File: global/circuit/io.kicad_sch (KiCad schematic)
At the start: 8 parts, among them J1 AudioJack2_Ground, J2 AudioJack2_Ground, J3 USB4125-GF-A-0190, SW1 SW_DPDT_x2

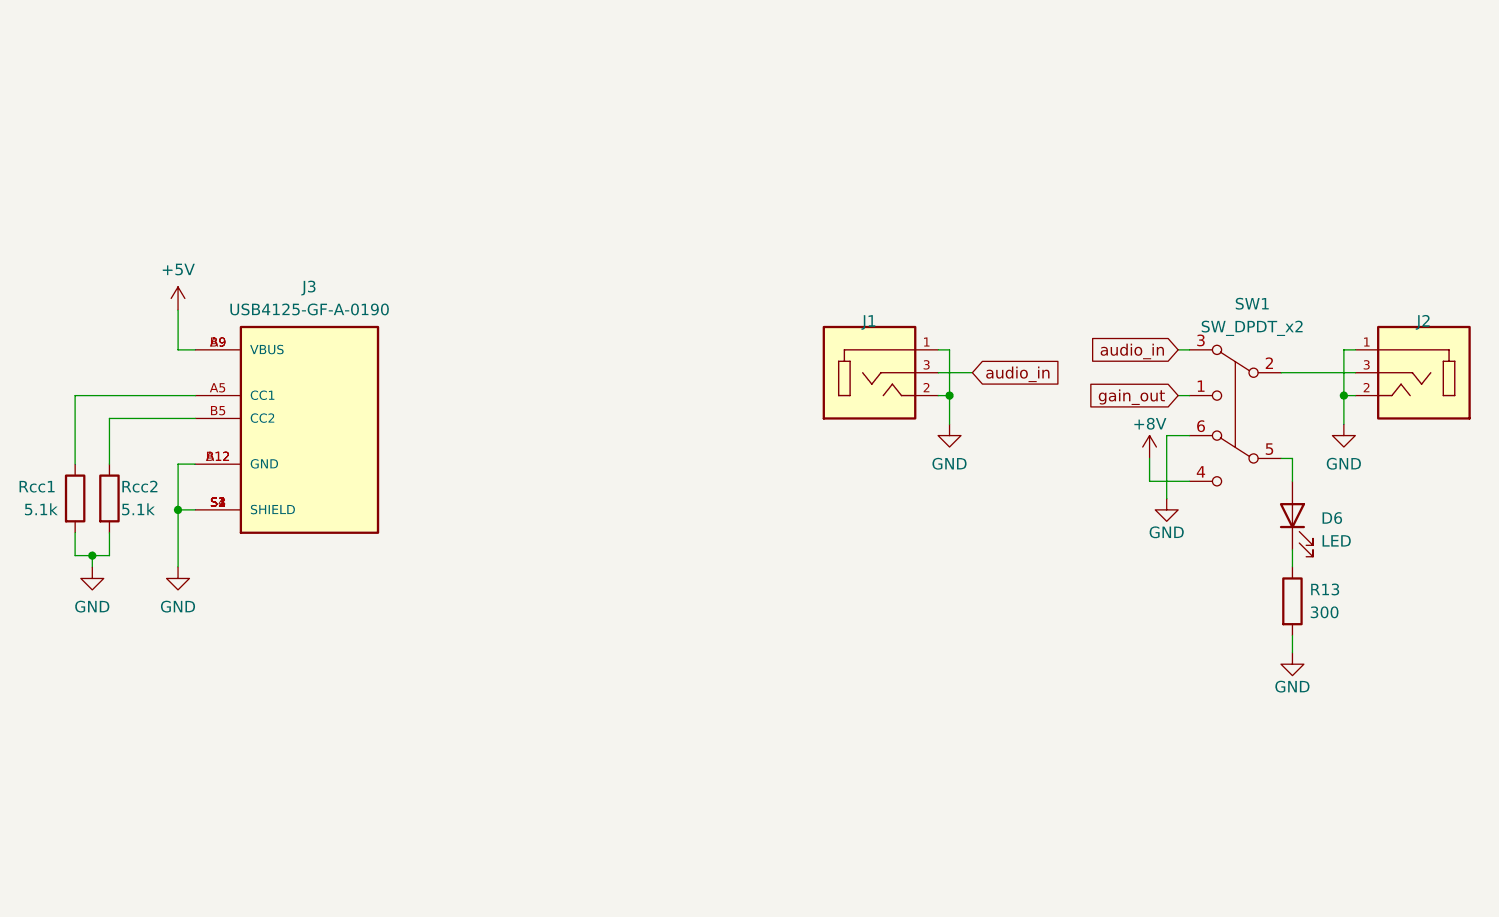
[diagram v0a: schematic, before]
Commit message: rework distortion circuit and simulations
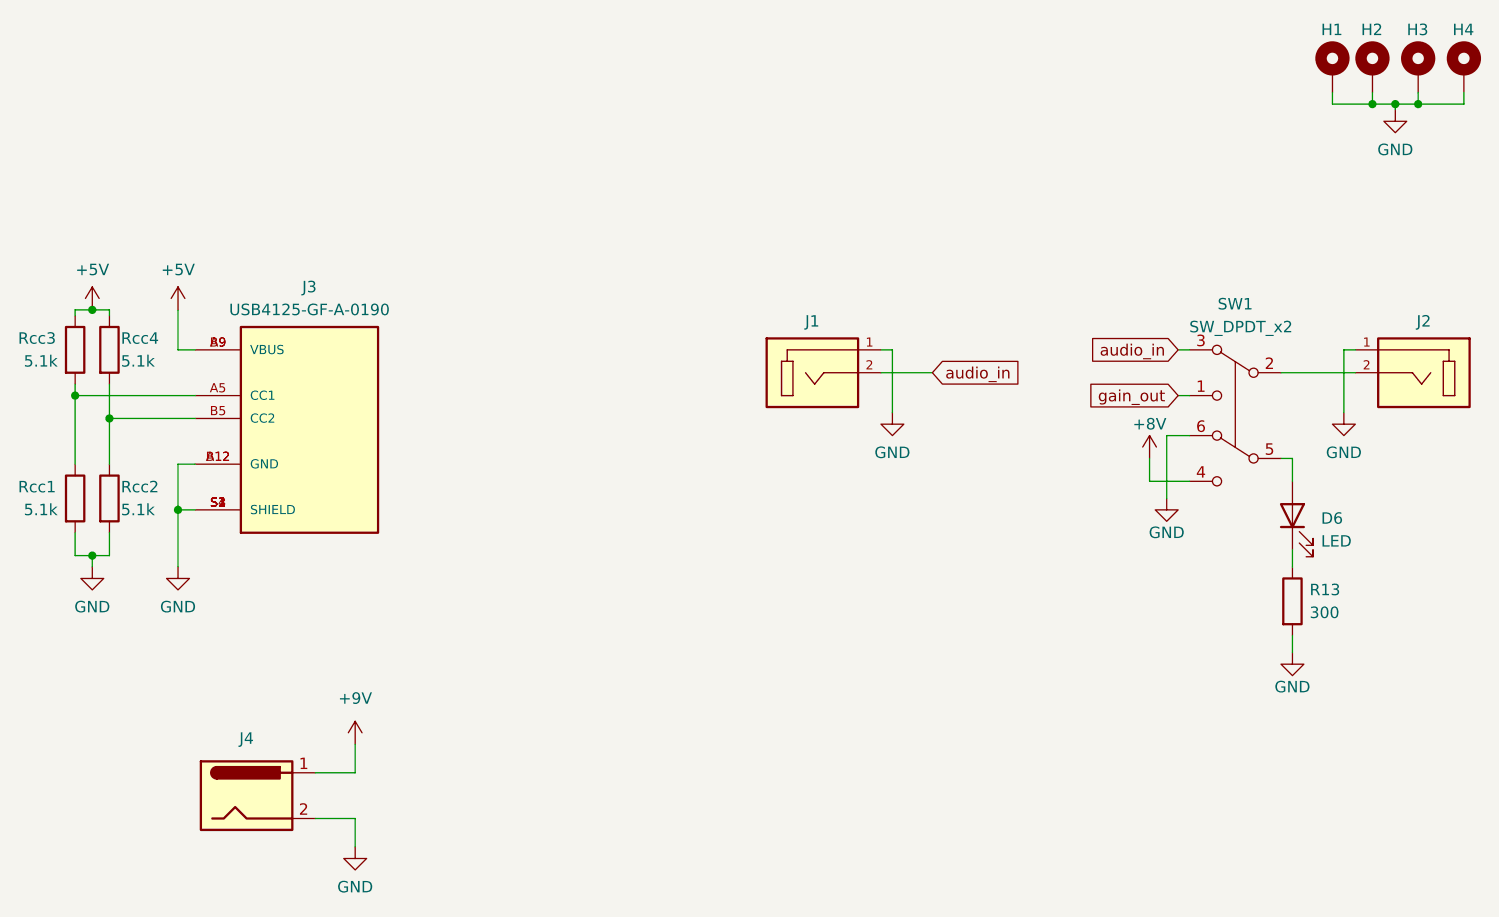
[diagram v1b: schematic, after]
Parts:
- added H1, H2, H3, H4: MountingHole_Pad, MountingHole:MountingHole_2.2mm_M2_DIN965_Pad_TopBottom, symbol Mechanical:MountingHole_Pad
- added J4: Barrel_Jack, Connector_PinHeader_2.54mm:PinHeader_1x02_P2.54mm_Vertical, symbol Connector:Barrel_Jack
- added Rcc3, Rcc4: 5.1k, Resistor_SMD:R_0805_2012Metric_Pad1.20x1.40mm_HandSolder, symbol Device:R
- D6: footprint effect_pedal:FB_28C0236-0EW-10 -> Connector_PinHeader_2.54mm:PinHeader_1x02_P2.54mm_Vertical
- J1, J2: footprint effect_pedal:CUI_SJ-3523-SMT-TR-V2 -> Connector_PinHeader_2.54mm:PinHeader_1x02_P2.54mm_Vertical; symbol effect_pedal:SJ-3523-SMT-TR -> effect_pedal:audio_jack_1_GND
- SW1: footprint effect_pedal:SF12011F020220RL050 -> Connector_PinHeader_2.54mm:PinHeader_2x03_P2.54mm_Vertical
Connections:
- net +5V: now also Rcc3.1, Rcc4.1
- net GND: now also H1.1, H2.1, H3.1, H4.1, J4.2; no longer J1.2, J2.2
- net audio_in: now also J1.2; no longer J1.3
- net at J3.A5 (CC1), Rcc1.1: now also Rcc3.2
- net at J3.B5 (CC2), Rcc2.1: now also Rcc4.2
- net at SW1.2: now also J2.2; no longer J2.3
- new net +9V: J4.1

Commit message: distortion rev 3
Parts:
- D6: footprint Connector_PinHeader_2.54mm:PinHeader_1x02_P2.54mm_Vertical -> effect_pedal:led_wired_1_pin
- J1: footprint Connector_PinHeader_2.54mm:PinHeader_1x02_P2.54mm_Vertical -> effect_pedal:audio_jack_wired
- J2: footprint Connector_PinHeader_2.54mm:PinHeader_1x02_P2.54mm_Vertical -> effect_pedal:audio_jack_wired_shield_only
- SW1: footprint Connector_PinHeader_2.54mm:PinHeader_2x03_P2.54mm_Vertical -> effect_pedal:switch_wired_reduced
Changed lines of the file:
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@@
       (effects (font (size 1.27 1.27)) hide)
     )
-    (property "Footprint" "Connector_PinHeader_2.54mm:PinHeader_1x02_P2.54mm_Vertical" (id 2) (at 111.125 55.88 0)
+    (property "Footprint" "effect_pedal:audio_jack_wired" (id 2) (at 111.125 55.88 0)
       (effects (font (size 1.27 1.27)) hide)
     )
@@
       (effects (font (size 1.27 1.27)) hide)
     )
-    (property "Footprint" "Connector_PinHeader_2.54mm:PinHeader_1x02_P2.54mm_Vertical" (id 2) (at 179.07 55.88 0)
+    (property "Footprint" "effect_pedal:audio_jack_wired_shield_only" (id 2) (at 179.07 55.88 0)
       (effects (font (size 1.27 1.27)) hide)
     )
@@
     (property "Reference" "SW1" (id 0) (at 158.115 48.26 0))
     (property "Value" "SW_DPDT_x2" (id 1) (at 158.75 50.8 0))
-    (property "Footprint" "Connector_PinHeader_2.54mm:PinHeader_2x03_P2.54mm_Vertical" (id 2) (at 133.35 53.34 0)
+    (property "Footprint" "effect_pedal:switch_wired_reduced" (id 2) (at 133.35 53.34 0)
       (effects (font (size 1.27 1.27)) (justify left) hide)
     )
@@
       (effects (font (size 1.27 1.27)) (justify right))
     )
-    (property "Footprint" "Connector_PinHeader_2.54mm:PinHeader_1x02_P2.54mm_Vertical" (id 2) (at 164.465 71.755 0)
-      (effects (font (size 1.27 1.27)) hide)
-    )
+    (property "Footprint" "effect_pedal:led_wired_1_pin" (id 2) (at 164.465 71.755 0)
+      (effects (font (size 1.27 1.27)) hide)
+    )

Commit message: rework global circuits
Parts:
- J?: renamed from J4; footprint Connector_PinHeader_2.54mm:PinHeader_1x02_P2.54mm_Vertical -> effect_pedal:barrel_jack_wired
- J?: renamed from J2; footprint effect_pedal:audio_jack_wired_shield_only -> effect_pedal:audio_jack_wired
- SW?: renamed from SW1; footprint effect_pedal:switch_wired_reduced -> effect_pedal:switch_wired
- renumbered D6 to D?, H3 to H?, H4 to H?, H1 to H?, H2 to H?, J1 to J?, J3 to J?, R13 to R?, Rcc4 to Rcc?, Rcc1 to Rcc?, Rcc2 to Rcc?, Rcc3 to Rcc?
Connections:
- net gain_out renamed effect_out
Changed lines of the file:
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@@
     )
   )
-  (global_label "gain_out" (shape input) (at 151.765 58.42 180) (fields_autoplaced)
+  (global_label "effect_out" (shape input) (at 151.765 58.42 180) (fields_autoplaced)
     (effects (font (size 1.27 1.27)) (justify right))
-    (property "Intersheet References" "${INTERSHEET_REFS}" (id 0) (at 141.3086 58.3406 0)
+    (property "Intersheet References" "${INTERSHEET_REFS}" (id 0) (at 139.9176 58.3406 0)
       (effects (font (size 1.27 1.27)) (justify right) hide)
     )
@@
   (symbol (lib_id "power:GND") (at 120.015 60.325 0) (unit 1)
     (in_bom yes) (on_board yes)
-    (property "Reference" "#PWR0109" (id 0) (at 120.015 66.675 0)
+    (property "Reference" "#PWR?" (id 0) (at 120.015 66.675 0)
       (effects (font (size 1.27 1.27)) hide)
     )
@@
   (symbol (lib_id "power:GND") (at 150.495 69.85 0) (unit 1)
     (in_bom yes) (on_board yes)
-    (property "Reference" "#PWR026" (id 0) (at 150.495 76.2 0)
+    (property "Reference" "#PWR?" (id 0) (at 150.495 76.2 0)
       (effects (font (size 1.27 1.27)) hide)
     )
@@
   (symbol (lib_id "power:+5V") (at 31.115 48.895 0) (unit 1)
     (in_bom yes) (on_board yes)
-    (property "Reference" "#PWR028" (id 0) (at 31.115 52.705 0)
+    (property "Reference" "#PWR?" (id 0) (at 31.115 52.705 0)
       (effects (font (size 1.27 1.27)) hide)
     )
@@
   (symbol (lib_id "Connector:Barrel_Jack") (at 48.26 102.87 0) (unit 1)
     (in_bom yes) (on_board yes)
-    (property "Reference" "J4" (id 0) (at 48.26 96.52 0))
+    (property "Reference" "J?" (id 0) (at 48.26 96.52 0))
     (property "Value" "Barrel_Jack" (id 1) (at 48.26 96.52 0)
       (effects (font (size 1.27 1.27)) hide)
     )
-    (property "Footprint" "Connector_PinHeader_2.54mm:PinHeader_1x02_P2.54mm_Vertical" (id 2) (at 49.53 103.886 0)
+    (property "Footprint" "effect_pedal:barrel_jack_wired" (id 2) (at 49.53 103.886 0)
       (effects (font (size 1.27 1.27)) hide)
     )
@@
   (symbol (lib_id "Device:R") (at 33.02 53.34 0) (unit 1)
     (in_bom yes) (on_board yes)
-    (property "Reference" "Rcc4" (id 0) (at 34.29 52.07 0)
+    (property "Reference" "Rcc?" (id 0) (at 34.29 52.07 0)
       (effects (font (size 1.27 1.27)) (justify left))
     )
@@
   (symbol (lib_id "power:GND") (at 40.64 77.47 0) (unit 1)
     (in_bom yes) (on_board yes)
-    (property "Reference" "#PWR0113" (id 0) (at 40.64 83.82 0)
+    (property "Reference" "#PWR?" (id 0) (at 40.64 83.82 0)
       (effects (font (size 1.27 1.27)) hide)
     )
@@
   (symbol (lib_id "power:+9V") (at 60.325 97.155 0) (unit 1)
     (in_bom yes) (on_board yes) (fields_autoplaced)
-    (property "Reference" "#PWR0101" (id 0) (at 60.325 100.965 0)
+    (property "Reference" "#PWR?" (id 0) (at 60.325 100.965 0)
       (effects (font (size 1.27 1.27)) hide)
     )
@@
   (symbol (lib_id "Mechanical:MountingHole_Pad") (at 178.435 22.225 0) (unit 1)
     (in_bom yes) (on_board yes)
-    (property "Reference" "H3" (id 0) (at 177.165 17.78 0)
+    (property "Reference" "H?" (id 0) (at 177.165 17.78 0)
       (effects (font (size 1.27 1.27)) (justify left))
     )
@@
   (symbol (lib_id "power:GND") (at 170.18 60.325 0) (unit 1)
     (in_bom yes) (on_board yes)
-    (property "Reference" "#PWR0108" (id 0) (at 170.18 66.675 0)
+    (property "Reference" "#PWR?" (id 0) (at 170.18 66.675 0)
       (effects (font (size 1.27 1.27)) hide)
     )
@@
   (symbol (lib_id "Device:R") (at 164.465 81.28 0) (unit 1)
     (in_bom yes) (on_board yes) (fields_autoplaced)
-    (property "Reference" "R13" (id 0) (at 166.37 80.0099 0)
+    (property "Reference" "R?" (id 0) (at 166.37 80.0099 0)
       (effects (font (size 1.27 1.27)) (justify left))
     )
@@
   (symbol (lib_id "Mechanical:MountingHole_Pad") (at 183.515 22.225 0) (unit 1)
     (in_bom yes) (on_board yes)
-    (property "Reference" "H4" (id 0) (at 182.245 17.78 0)
+    (property "Reference" "H?" (id 0) (at 182.245 17.78 0)
       (effects (font (size 1.27 1.27)) (justify left))
     )
@@
   (symbol (lib_id "Device:R") (at 29.21 69.85 0) (unit 1)
     (in_bom yes) (on_board yes)
-    (property "Reference" "Rcc1" (id 0) (at 22.86 68.58 0)
+    (property "Reference" "Rcc?" (id 0) (at 22.86 68.58 0)
       (effects (font (size 1.27 1.27)) (justify left))
     )
@@
   (symbol (lib_id "power:+5V") (at 40.64 48.895 0) (unit 1)
     (in_bom yes) (on_board yes)
-    (property "Reference" "#PWR0114" (id 0) (at 40.64 52.705 0)
+    (property "Reference" "#PWR?" (id 0) (at 40.64 52.705 0)
       (effects (font (size 1.27 1.27)) hide)
     )
@@
   (symbol (lib_id "effect_pedal:audio_jack_1_GND") (at 111.125 55.88 0) (unit 1)
     (in_bom yes) (on_board yes)
-    (property "Reference" "J1" (id 0) (at 111.125 50.165 0))
+    (property "Reference" "J?" (id 0) (at 111.125 50.165 0))
     (property "Value" "AudioJack2_Ground" (id 1) (at 110.49 49.53 0)
       (effects (font (size 1.27 1.27)) hide)
@@
   (symbol (lib_id "effect_pedal:USB4125-GF-A-0190_REVA2") (at 55.245 60.96 0) (unit 1)
     (in_bom yes) (on_board yes)
-    (property "Reference" "J3" (id 0) (at 55.245 46.355 0))
+    (property "Reference" "J?" (id 0) (at 55.245 46.355 0))
     (property "Value" "USB4125-GF-A-0190" (id 1) (at 55.245 48.895 0))
     (property "Footprint" "GCT_USB4125-GF-A-0190_REVA2" (id 2) (at 55.245 60.96 0)
@@
   (symbol (lib_id "effect_pedal:audio_jack_1_GND") (at 179.07 55.88 0) (mirror y) (unit 1)
     (in_bom yes) (on_board yes)
-    (property "Reference" "J2" (id 0) (at 179.07 50.165 0))
+    (property "Reference" "J?" (id 0) (at 179.07 50.165 0))
     (property "Value" "AudioJack2_Ground" (id 1) (at 179.705 49.53 0)
       (effects (font (size 1.27 1.27)) hide)
     )
-    (property "Footprint" "effect_pedal:audio_jack_wired_shield_only" (id 2) (at 179.07 55.88 0)
+    (property "Footprint" "effect_pedal:audio_jack_wired" (id 2) (at 179.07 55.88 0)
       (effects (font (size 1.27 1.27)) hide)
     )
@@
   (symbol (lib_id "Mechanical:MountingHole_Pad") (at 168.91 22.225 0) (unit 1)
     (in_bom yes) (on_board yes)
-    (property "Reference" "H1" (id 0) (at 167.64 17.78 0)
+    (property "Reference" "H?" (id 0) (at 167.64 17.78 0)
       (effects (font (size 1.27 1.27)) (justify left))
     )
@@
   (symbol (lib_id "power:GND") (at 31.115 77.47 0) (unit 1)
     (in_bom yes) (on_board yes)
-    (property "Reference" "#PWR0112" (id 0) (at 31.115 83.82 0)
+    (property "Reference" "#PWR?" (id 0) (at 31.115 83.82 0)
       (effects (font (size 1.27 1.27)) hide)
     )
@@
   (symbol (lib_id "power:GND") (at 175.895 26.67 0) (unit 1)
     (in_bom yes) (on_board yes) (fields_autoplaced)
-    (property "Reference" "#PWR05" (id 0) (at 175.895 33.02 0)
+    (property "Reference" "#PWR?" (id 0) (at 175.895 33.02 0)
       (effects (font (size 1.27 1.27)) hide)
     )
@@
   (symbol (lib_id "effect_pedal:SF12011F-0202-20R-L-050") (at 160.02 55.88 0) (mirror y) (unit 1)
     (in_bom yes) (on_board yes)
-    (property "Reference" "SW1" (id 0) (at 158.115 48.26 0))
+    (property "Reference" "SW?" (id 0) (at 158.115 48.26 0))
     (property "Value" "SW_DPDT_x2" (id 1) (at 158.75 50.8 0))
-    (property "Footprint" "effect_pedal:switch_wired_reduced" (id 2) (at 133.35 53.34 0)
+    (property "Footprint" "effect_pedal:switch_wired" (id 2) (at 133.35 53.34 0)
       (effects (font (size 1.27 1.27)) (justify left) hide)
     )
@@
   (symbol (lib_id "power:GND") (at 60.325 108.585 0) (unit 1)
     (in_bom yes) (on_board yes) (fields_autoplaced)
-    (property "Reference" "#PWR0105" (id 0) (at 60.325 114.935 0)
+    (property "Reference" "#PWR?" (id 0) (at 60.325 114.935 0)
       (effects (font (size 1.27 1.27)) hide)
     )
@@
   (symbol (lib_id "power:GND") (at 164.465 86.995 0) (unit 1)
     (in_bom yes) (on_board yes)
-    (property "Reference" "#PWR027" (id 0) (at 164.465 93.345 0)
+    (property "Reference" "#PWR?" (id 0) (at 164.465 93.345 0)
       (effects (font (size 1.27 1.27)) hide)
     )
@@
   (symbol (lib_id "Device:LED") (at 164.465 71.755 90) (unit 1)
     (in_bom yes) (on_board yes) (fields_autoplaced)
-    (property "Reference" "D6" (id 0) (at 167.64 72.0724 90)
+    (property "Reference" "D?" (id 0) (at 167.64 72.0724 90)
       (effects (font (size 1.27 1.27)) (justify right))
     )
@@
   (symbol (lib_id "Mechanical:MountingHole_Pad") (at 173.355 22.225 0) (unit 1)
     (in_bom yes) (on_board yes)
-    (property "Reference" "H2" (id 0) (at 172.085 17.78 0)
+    (property "Reference" "H?" (id 0) (at 172.085 17.78 0)
       (effects (font (size 1.27 1.27)) (justify left))
     )
@@
   (symbol (lib_id "Device:R") (at 33.02 69.85 0) (unit 1)
     (in_bom yes) (on_board yes)
-    (property "Reference" "Rcc2" (id 0) (at 34.29 68.58 0)
+    (property "Reference" "Rcc?" (id 0) (at 34.29 68.58 0)
       (effects (font (size 1.27 1.27)) (justify left))
     )
@@
   (symbol (lib_id "Device:R") (at 29.21 53.34 0) (unit 1)
     (in_bom yes) (on_board yes)
-    (property "Reference" "Rcc3" (id 0) (at 22.86 52.07 0)
+    (property "Reference" "Rcc?" (id 0) (at 22.86 52.07 0)
       (effects (font (size 1.27 1.27)) (justify left))
     )
@@
   (symbol (lib_id "power:+8V") (at 148.59 65.405 0) (unit 1)
     (in_bom yes) (on_board yes)
-    (property "Reference" "#PWR025" (id 0) (at 148.59 69.215 0)
-      (effects (font (size 1.27 1.27)) hide)
-    )
+    (property "Reference" "#PWR?" (id 0) (at 148.59 69.215 0)
+      (effects (font (size 1.27 1.27)) hide)
+    )
